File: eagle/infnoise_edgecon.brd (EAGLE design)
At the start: 36.3 x 12.2 mm, 28 parts, among them SW1 MC74VHC1G66DFT1G, SW2 MC74VHC1G66DFT1G, X1 USB

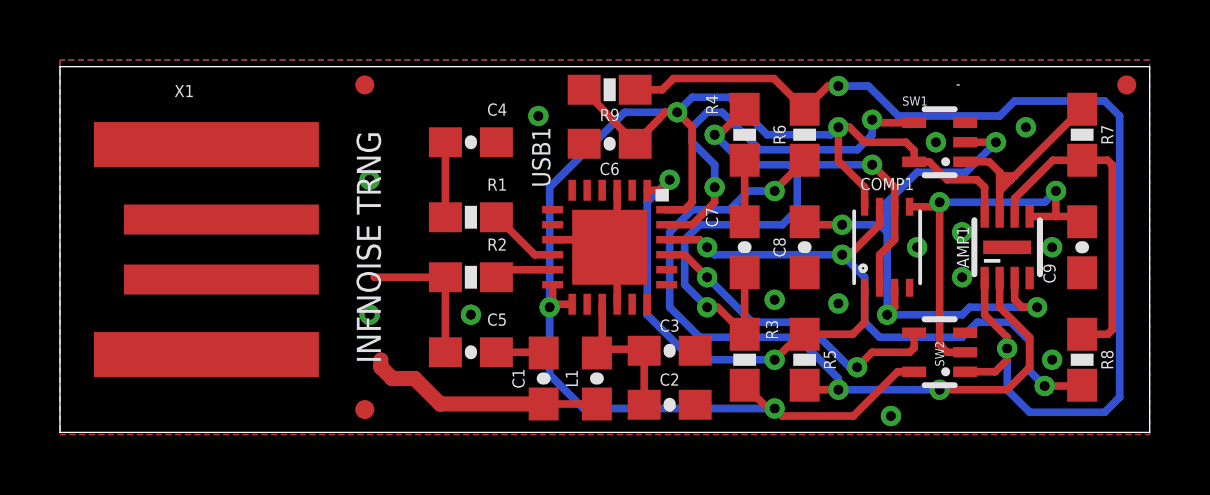
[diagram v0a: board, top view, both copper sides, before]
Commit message: Updated README to use modular noise multiplier
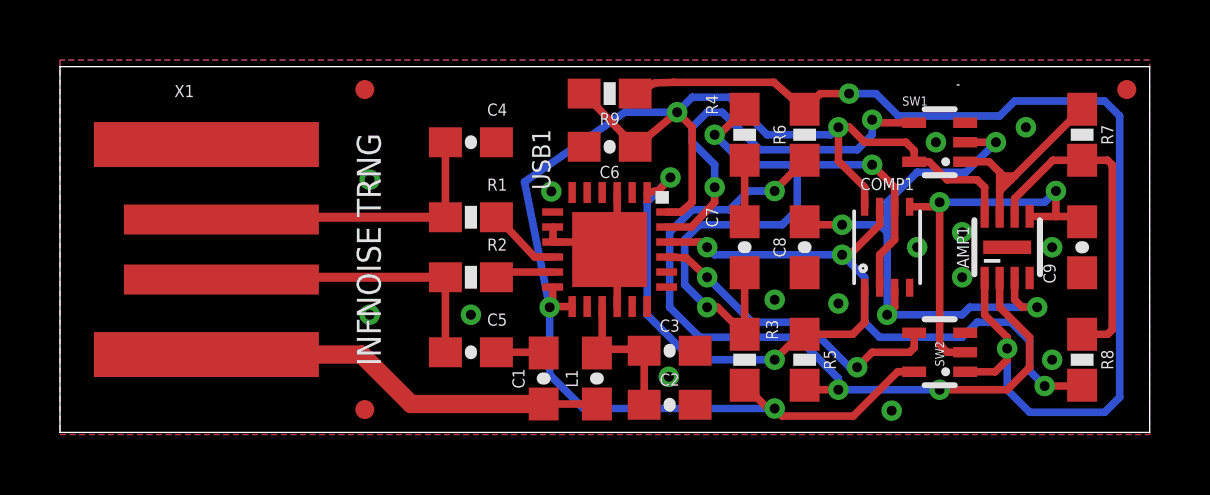
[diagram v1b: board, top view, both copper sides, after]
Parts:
- moved FID2 0.15 mm to (10.2, 11.4)
- moved FID3 0.15 mm to (35.6, 11.4)
- moved R9 0.13 mm to (18.3, 11.3)
- moved C6 0.10 mm to (18.3, 9.52)
- moved USB1 0.08 mm to (18.3, 6.10)
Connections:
- net GND: now also X1.GND
- net USB_M: now also X1.USB_M
- net USB_P: now also X1.USB_P
- net VCCIN: now also X1.5V
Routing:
- net USB_P: track 2.60 -> 10.1 mm
- net VCCIN: track 7.95 -> 13.7 mm
- net USB_M: track 4.88 -> 10.00 mm
- net VCC33: track 52.2 -> 52.9 mm
- net GND: track 9.64 -> 10.2 mm, vias 14 -> 15

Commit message: Cleaned up edge connector board a bit
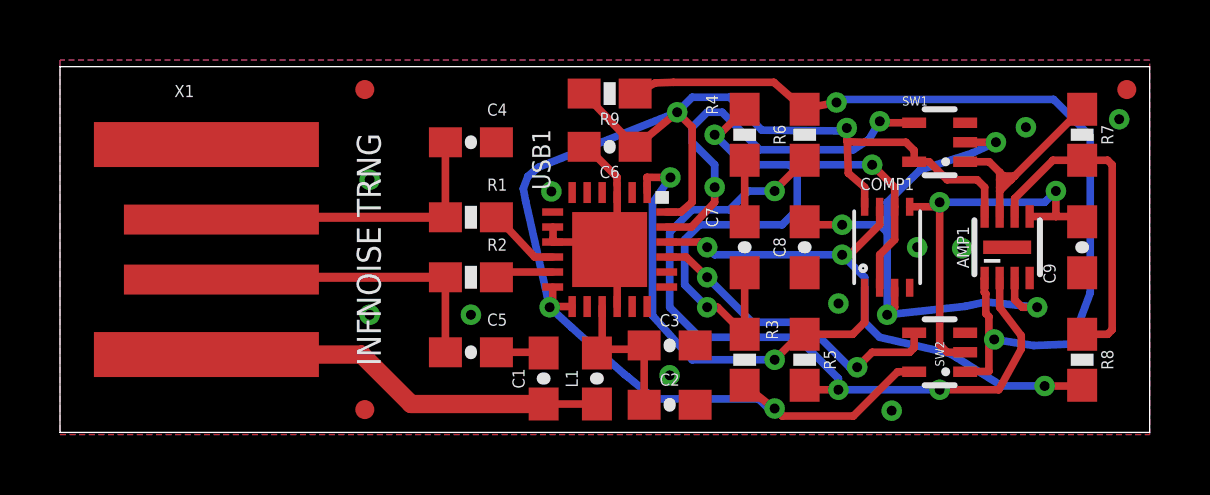
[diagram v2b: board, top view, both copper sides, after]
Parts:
- moved C3 0.18 mm to (20.3, 2.90)
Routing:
- net AMP1OUT: track 37.1 -> 30.0 mm
- net VCC33: track 52.9 -> 51.3 mm
- net COMP2: track 20.0 -> 18.7 mm
- net GND: track 10.2 -> 11.4 mm, vias 15 -> 11
- net FB1: track 26.4 -> 25.7 mm
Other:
- outline, holes or cut-outs redrawn
